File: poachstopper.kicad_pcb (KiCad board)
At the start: 2 copper layers, 50 x 38 mm, 9 parts, among them J1 XT60PW-M, J2 XT60PW-M, K1 G2RL-1A-E DC24, U2 NE555DR-MS

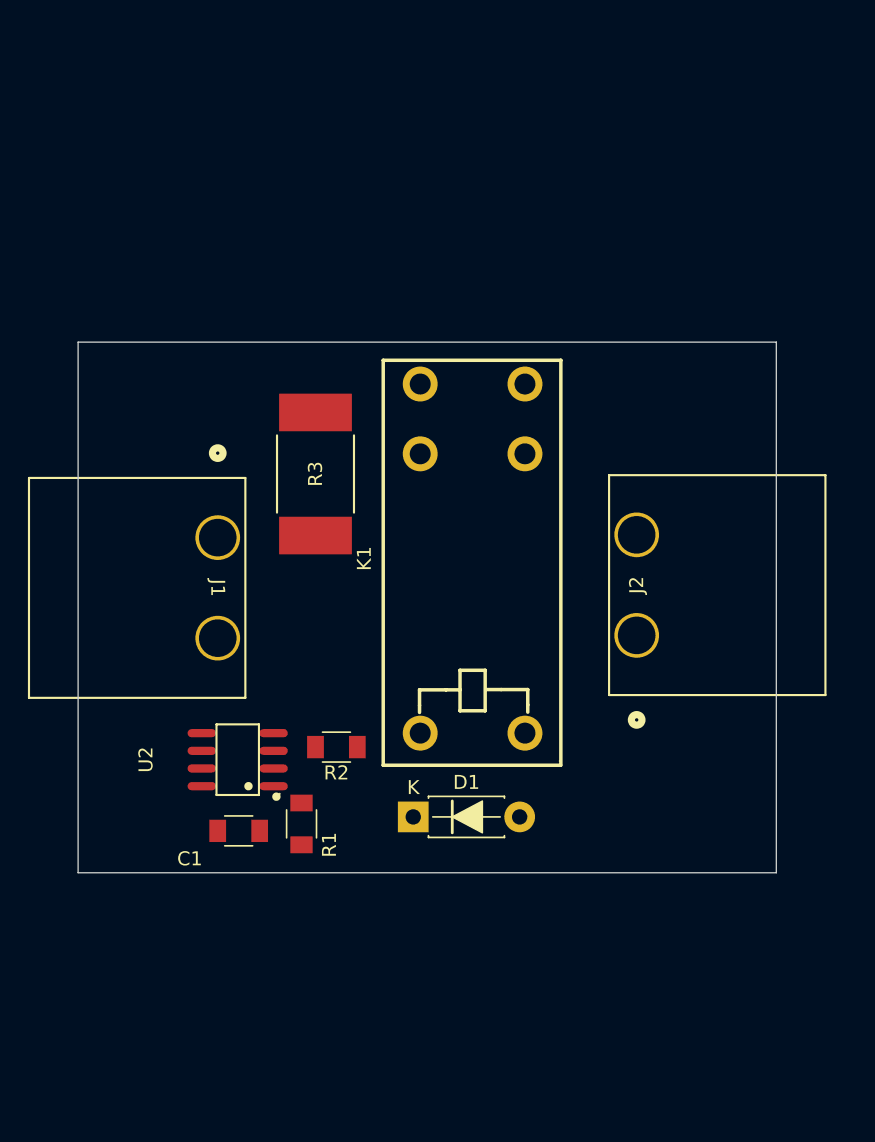
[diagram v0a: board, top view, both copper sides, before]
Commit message: circuit cleanup, functionality finalized, BOM
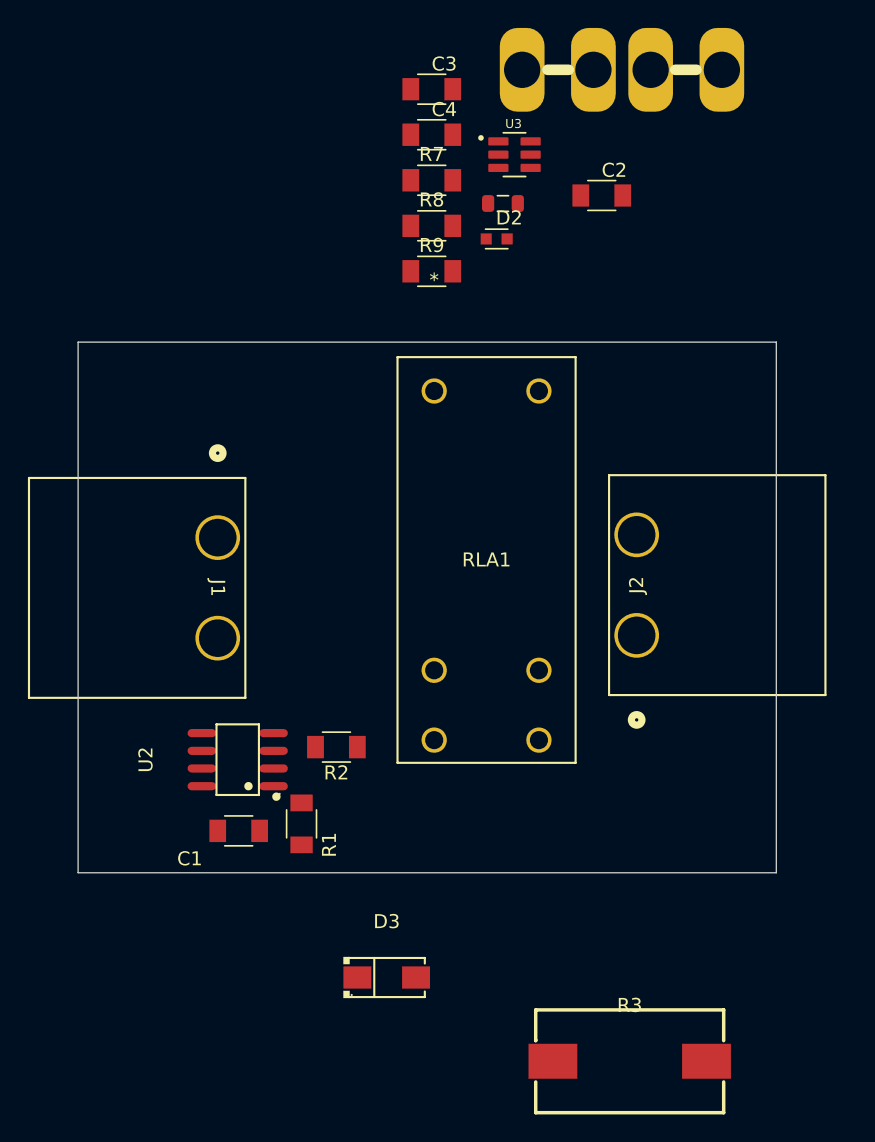
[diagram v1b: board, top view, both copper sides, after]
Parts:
- removed D1: 1N4007, PCM_Diode_THT_AKL:D_DO-41_SOD81_P7.62mm_Horizontal
- removed K1: G2RL-1A-E DC24, kicad-import:RELAY-TH_G2RL-1A-E
- added C2: 100nF, PCM_fab:C_1206, F.Cu at (168.5, 56.5)
- added C3: 10uF, PCM_fab:C_1206, F.Cu at (156.3, 48.9)
- added C4: 10uF, PCM_fab:C_1206, F.Cu at (156.3, 52.1)
- added D2: 60V/1A, PCM_fab:Diode_Schottky_0603, F.Cu at (161.0, 59.6)
- added D3: 1N4007_C727081, kicad-import:SMA_L4.3-W2.5-LS5.0-RD, F.Cu at (153.1, 112.5)
- added F1: Blade Fuse, PCM_SparkFun-Fuse:Fuseholder_Automotive, F.Cu at (169.9, 47.5)
- added L1: 22uH, PCM_SparkFun-Coil:0805, F.Cu at (161.4, 57.1)
- added R7: 56.2k, PCM_fab:R_1206, F.Cu at (156.3, 55.4)
- added R8: 10k, PCM_fab:R_1206, F.Cu at (156.3, 58.7)
- added R9: 100k, PCM_fab:R_1206, F.Cu at (156.3, 61.9)
- added RLA1: G2RL-1A-E DC5, kicad-import:RELAY_G2RL-1A-E_DC5_OMR, F.Cu at (164.0, 94.7)
- added U3: LMR16006XDDCT, kicad-import:SOT95P280X110-6N, F.Cu at (162.2, 53.6)
- C1: value C_1206 -> 220nF
- R1: value 15k -> 1M
- R2: value R_1206 -> 10
- R3: value 10 -> SMW510RJT; footprint kicad-import:RES_3550_TEC-L -> kicad-import:RES-SMD_L13.5-W7.3
- moved R3 47.7 mm to (170.5, 118.5), turned to 0 degrees
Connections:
- R3 pad 2: Net-(K1-Pad5) -> /24V_FEED

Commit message: v0.1.0
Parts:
- added G***: LOGO, LOGO, F.Cu at (139.5, 76.5)
- moved C3 55.3 mm to (152.0, 104.0), turned to 180 degrees
- moved C4 46.0 mm to (139.5, 95.0)
- moved U3 44.2 mm to (144.1, 93.8), turned to 90 degrees
- moved C2 42.8 mm to (139.5, 88.0)
- moved L1 42.2 mm to (135.1, 90.0)
- moved F1 41.9 mm to (152.0, 85.3), turned to -90 degrees
- moved R8 40.6 mm to (135.5, 93.5), turned to -90 degrees
- moved R7 39.4 mm to (139.5, 91.0)
- moved D2 38.3 mm to (134.8, 87.5)
- moved J1 36.5 mm to (172.5, 99.5), turned to 90 degrees
- moved R9 28.6 mm to (144.5, 88.0)
- moved RLA1 23.1 mm to (158.5, 72.3), turned to 180 degrees
- moved R3 16.8 mm to (162.0, 104.0), turned to 180 degrees
- moved D3 11.6 mm to (148.0, 102.1), turned to -90 degrees
- moved J2 5.51 mm to (172.5, 82.7)
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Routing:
- net /24V_FEED: track 0.00 -> 74.6 mm
- net Net-(J1-Pad1): track 0.00 -> 32.1 mm
- net GND: track 0.00 -> 28.6 mm
- net 5V: track 0.00 -> 28.3 mm, vias 0 -> 2
- net Net-(F1-Pad1): track 0.00 -> 25.0 mm
- net /LATCH_CONTROL: track 0.00 -> 18.4 mm, vias 0 -> 1
- net Net-(U3-FB): track 0.00 -> 16.8 mm, vias 0 -> 2
- net Net-(D2-K): track 0.00 -> 15.8 mm
- net Net-(U2-THRES): track 0.00 -> 12.0 mm
- net Net-(U3-CB): track 0.00 -> 10.2 mm
- net Net-(U2-OUT): track 0.00 -> 9.50 mm
- net Net-(U3-SHDN): track 0.00 -> 5.10 mm
- added copper zone on B.Cu, net GND
- added copper zone on F.Cu, net GND
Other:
- board size 50 x 38 mm -> 49 x 41 mm
